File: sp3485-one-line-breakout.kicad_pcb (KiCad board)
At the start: 2 copper layers, 20.3 x 8.9 mm, 4 parts, among them J1 Conn_01x08, U1 SP3485CN

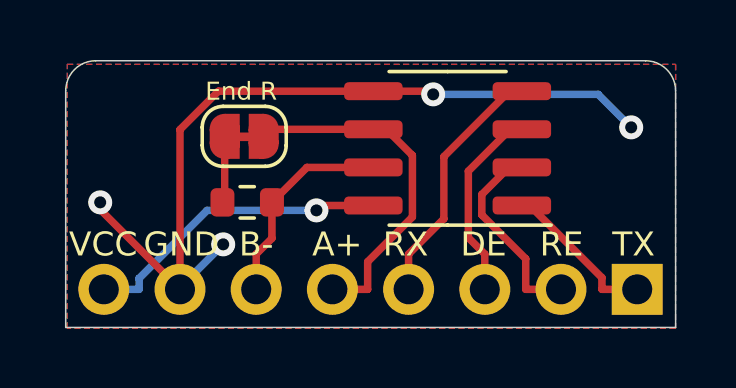
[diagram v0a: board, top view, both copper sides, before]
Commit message: Change resistor size and add capacitor
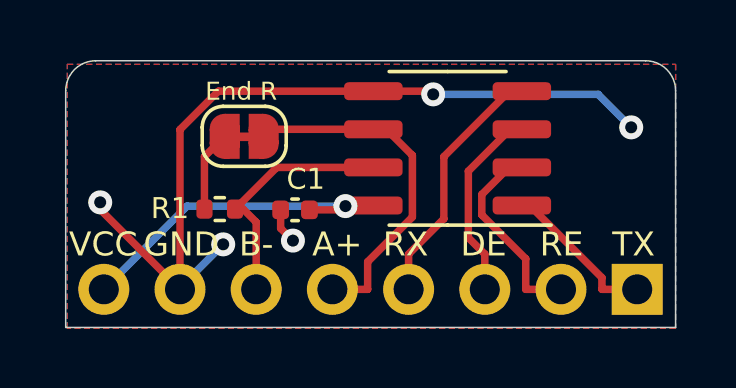
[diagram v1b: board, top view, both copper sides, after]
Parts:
- added C1: 0.1uf, Capacitor_SMD:C_0402_1005Metric, F.Cu at (145.0, 74.0)
- R1: footprint Resistor_SMD:R_0603_1608Metric -> Resistor_SMD:R_0402_1005Metric
- moved R1 0.94 mm to (142.5, 73.9)
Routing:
- net /B: track 6.98 -> 8.31 mm
- net GND: track 27.5 -> 28.7 mm, vias 4 -> 5
- net VCC: track 10.4 -> 11.4 mm

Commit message: Update revision to 2021.05
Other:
- board text added: "Rev2021.05"
- board text removed: "Rev2020.11"
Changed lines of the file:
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@@
     (effects (font (size 1.2 1.2) (thickness 0.3)) (justify mirror))
   )
-  (gr_text Rev2020.11 (at 153.45 73.5) (layer B.SilkS)
+  (gr_text Rev2021.05 (at 153.45 73.5) (layer B.SilkS)
     (effects (font (size 0.8 0.8) (thickness 0.15)) (justify mirror))
   )
